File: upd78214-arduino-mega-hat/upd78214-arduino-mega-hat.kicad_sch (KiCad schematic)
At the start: 13 parts, among them J1 Power, J2 PWM, J3 Analog, J4 PWM, J5 Analog, J6 Communication, J7 Digital, U1 upd78214-64p-qfp, Y1 4-12MHz

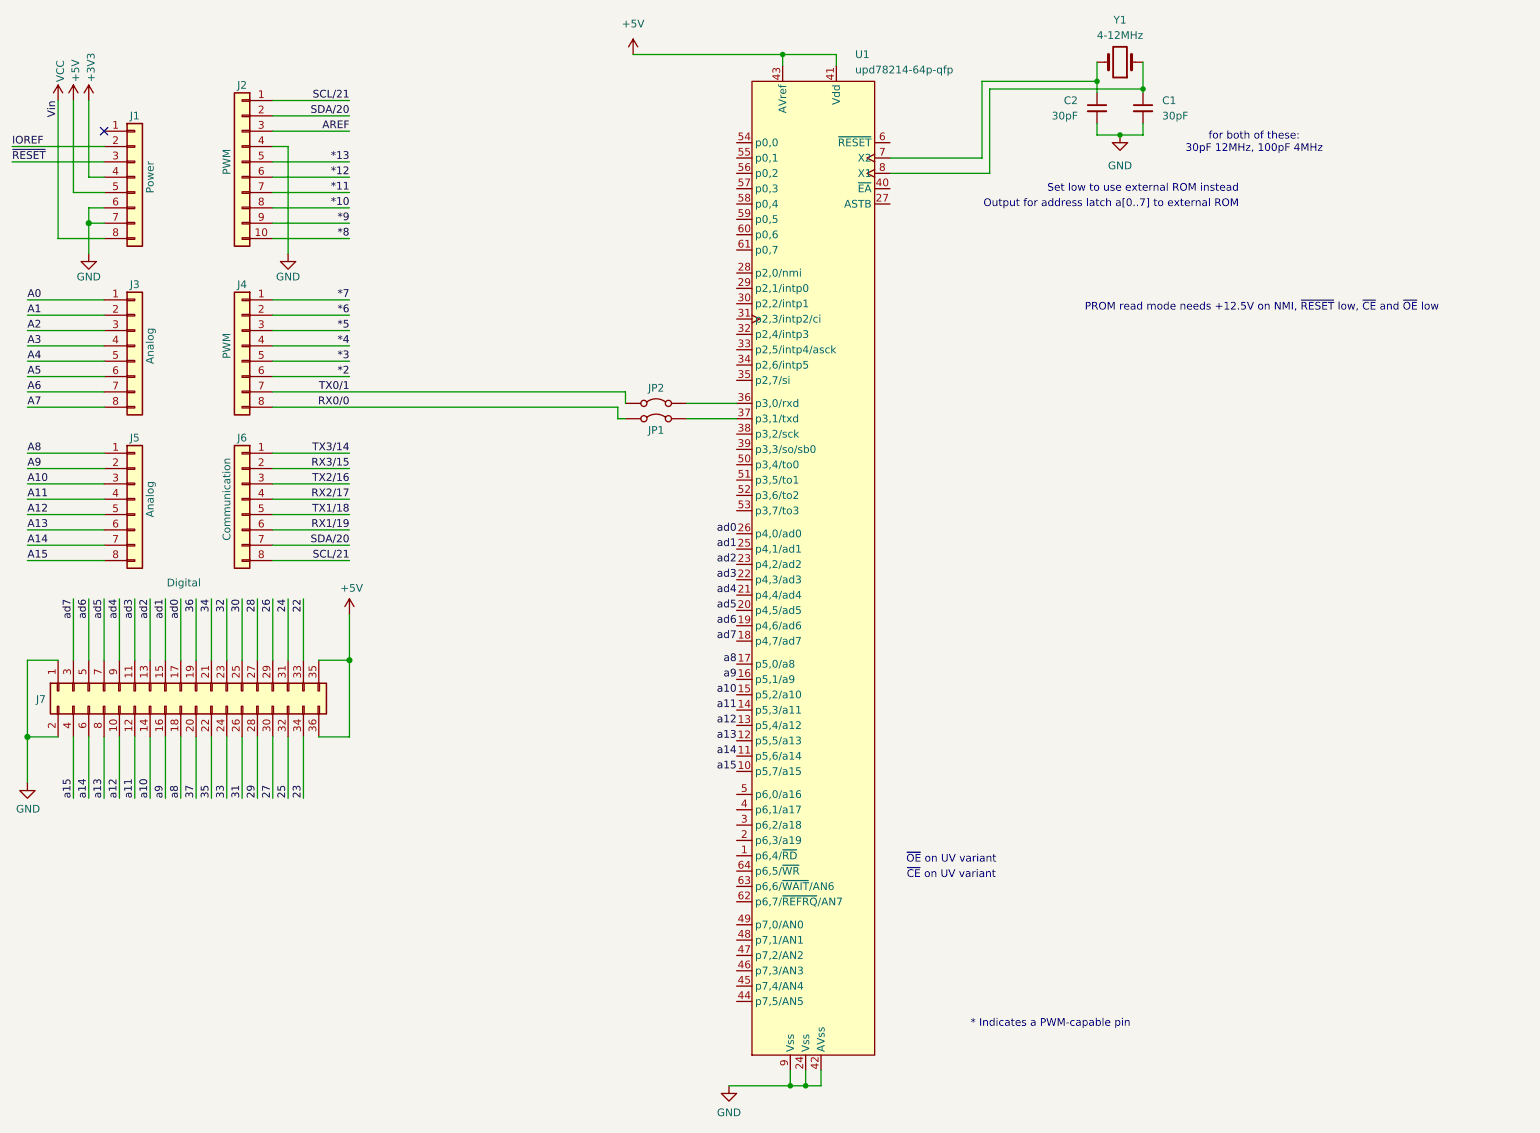
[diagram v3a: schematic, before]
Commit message: Applying programming mode notes
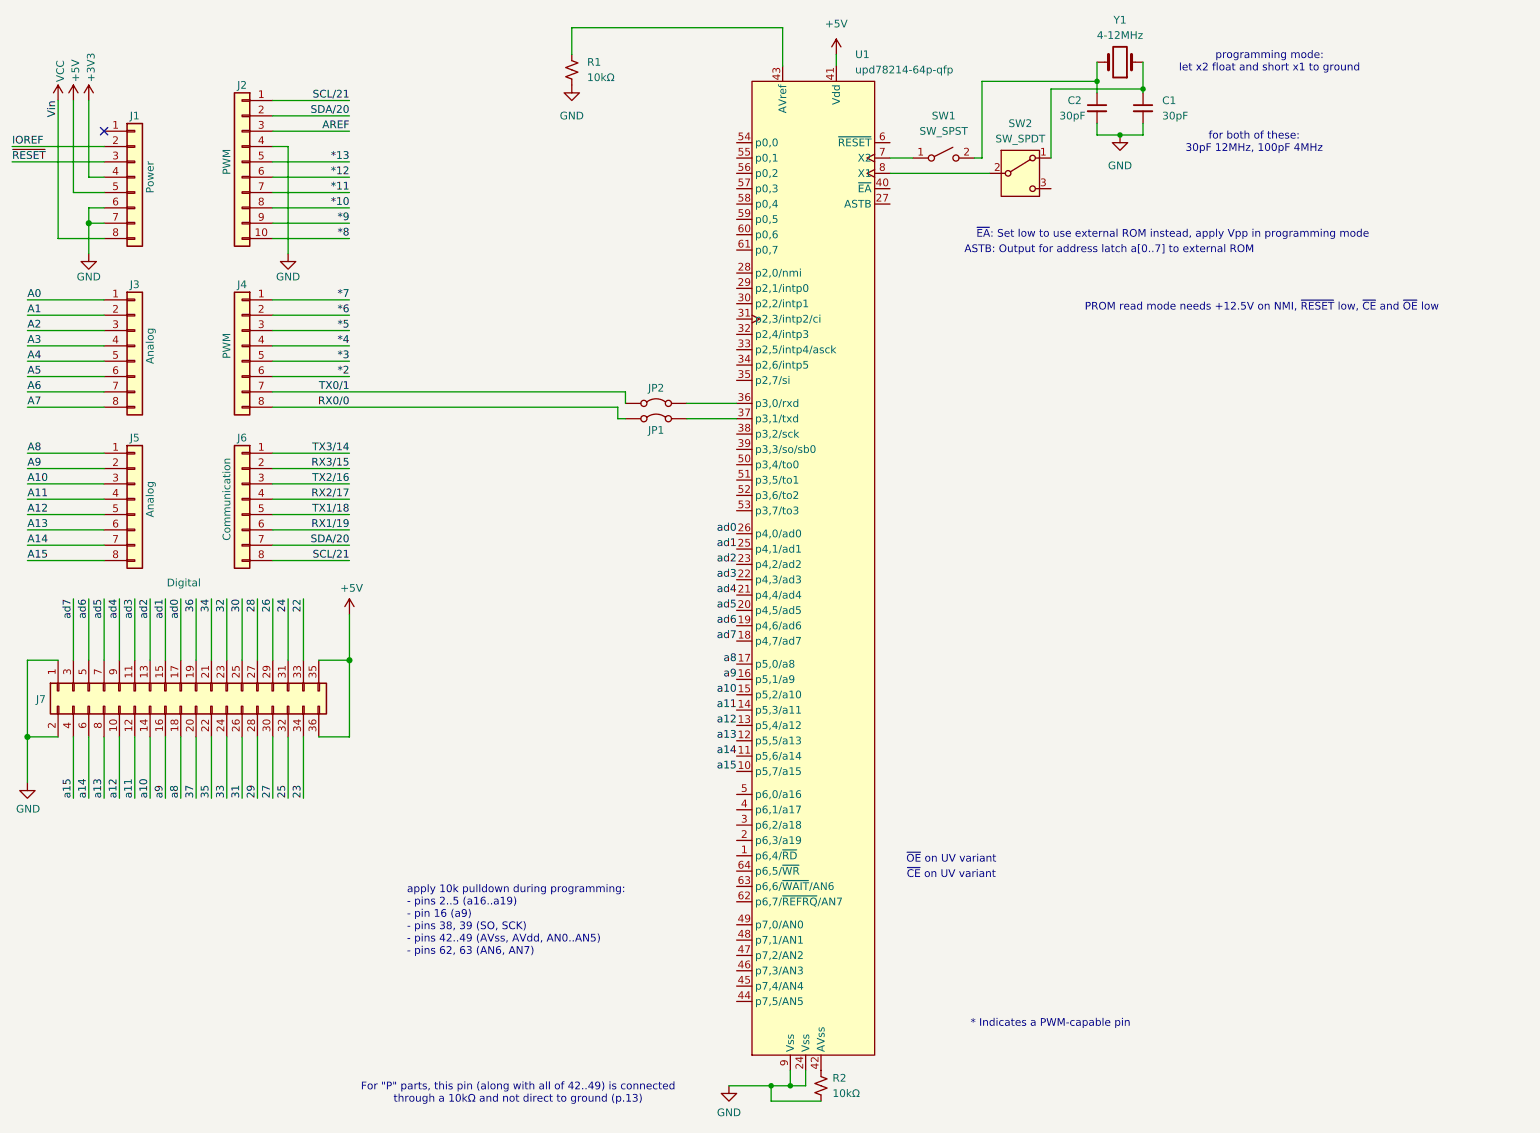
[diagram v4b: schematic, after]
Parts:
- added R1, R2: 10kΩ, symbol Device:R_Small_US
- added SW1: SW_SPST, symbol Switch:SW_SPST
- added SW2: SW_SPDT, symbol Switch:SW_SPDT
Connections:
- net +5V: no longer U1.43 (AVref)
- net GND: now also R1.2, R2.2; no longer U1.42 (AVss)
- net at C2.1, Y1.2: now also SW1.2 (B); no longer U1.7 (X2)
- net at C1.1, Y1.1: now also SW2.1 (A); no longer U1.8 (X1)
- new net: SW1.1 (A), U1.7 (X2)
- new net: R1.1, U1.43 (AVref)
- new net: R2.1, U1.42 (AVss)
- new net: SW2.2 (B), U1.8 (X1)
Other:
- note added: "ASTB: Output for address latch a[0..7] to external ROM"
- note added: "For "P" parts, this pin (along with all of 42..49) is connected through a 10kΩ and not direct to ground (p.13)"
- note added: "apply 10k pulldown during programming: - pins 2..5 (a16..a19) - pin 16 (a9) - pins 38, 39 (SO, SCK) - pins 42..49 (AVss, AVdd, AN0..AN5) - pins 62, 63 (AN6, AN7)"
- note added: "programming mode: let x2 float and short x1 to ground"
- note added: "~{EA}: Set low to use external ROM instead, apply Vpp in programming mode"
- note removed: "Output for address latch a[0..7] to external ROM"
- note removed: "Set low to use external ROM instead"
